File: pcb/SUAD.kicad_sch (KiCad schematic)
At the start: 18 parts, among them Q1 AO3401A, Q2 AO3401A, Q3 AO3401A, U1 Pico

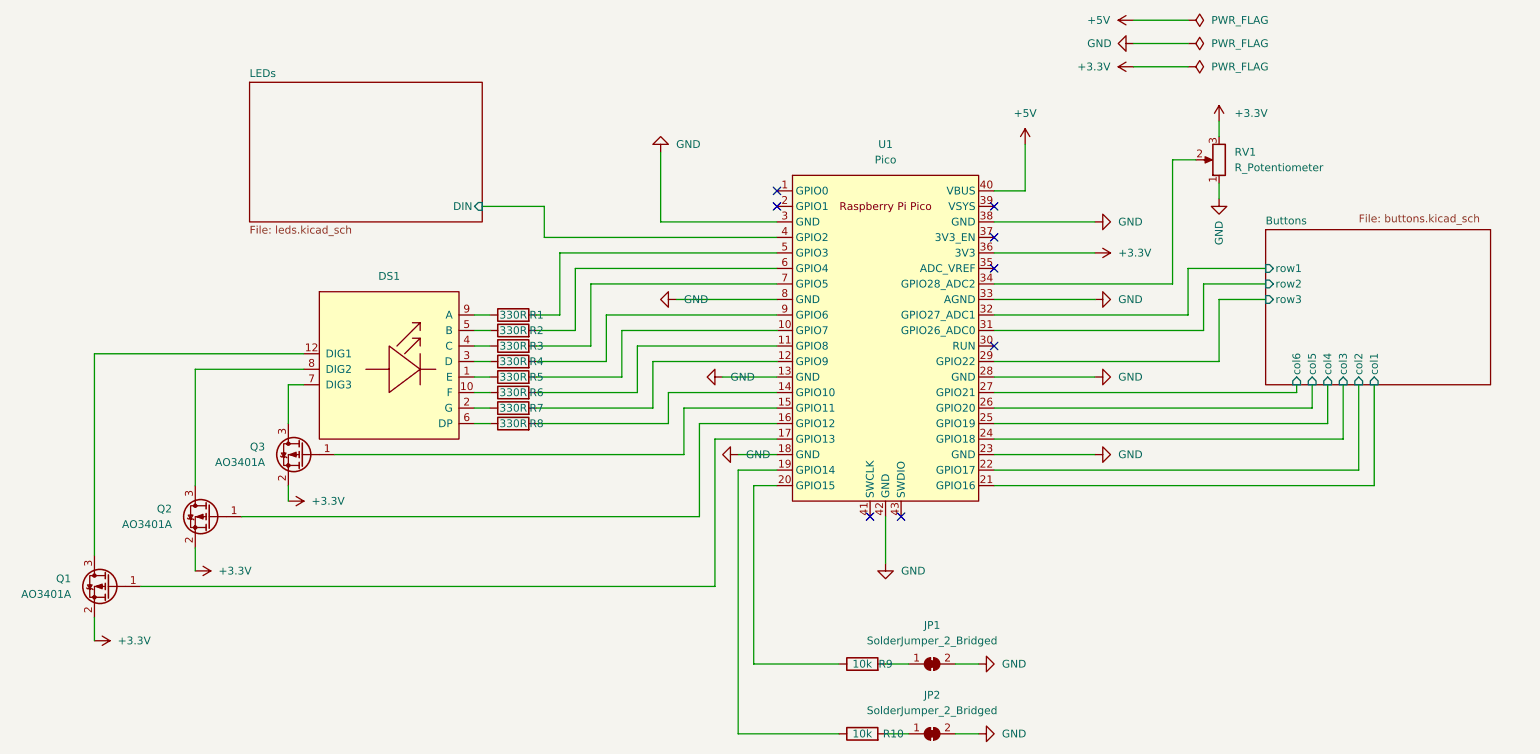
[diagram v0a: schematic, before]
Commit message: Silkscreen and footprint improvements
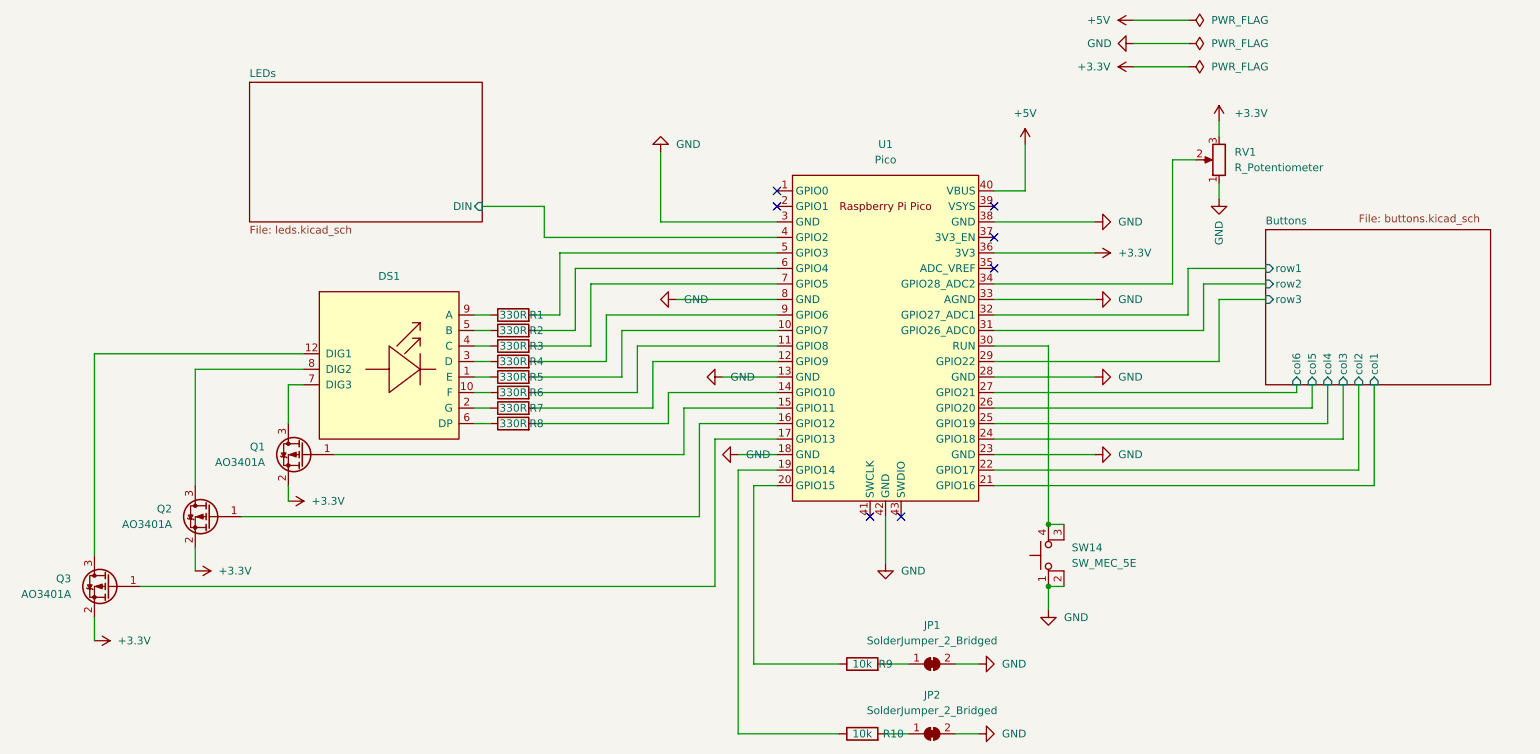
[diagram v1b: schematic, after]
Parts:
- added SW14: SW_MEC_5E, LCSC_parts:TS-1187A-B-A-B, symbol Switch:SW_MEC_5E
- renumbered Q3 to Q1, Q1 to Q3
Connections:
- net GND: now also SW14.1, SW14.2
- net at U1.30 (RUN): now also SW14.3 (K), SW14.4 (A)
- no-connect marks 8 -> 7
